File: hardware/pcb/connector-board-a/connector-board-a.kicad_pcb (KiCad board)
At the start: 2 copper layers, 23.1 x 39.1 mm, 2 parts, among them J1 DE9_Pins, J2 Conn_01x09_Pin

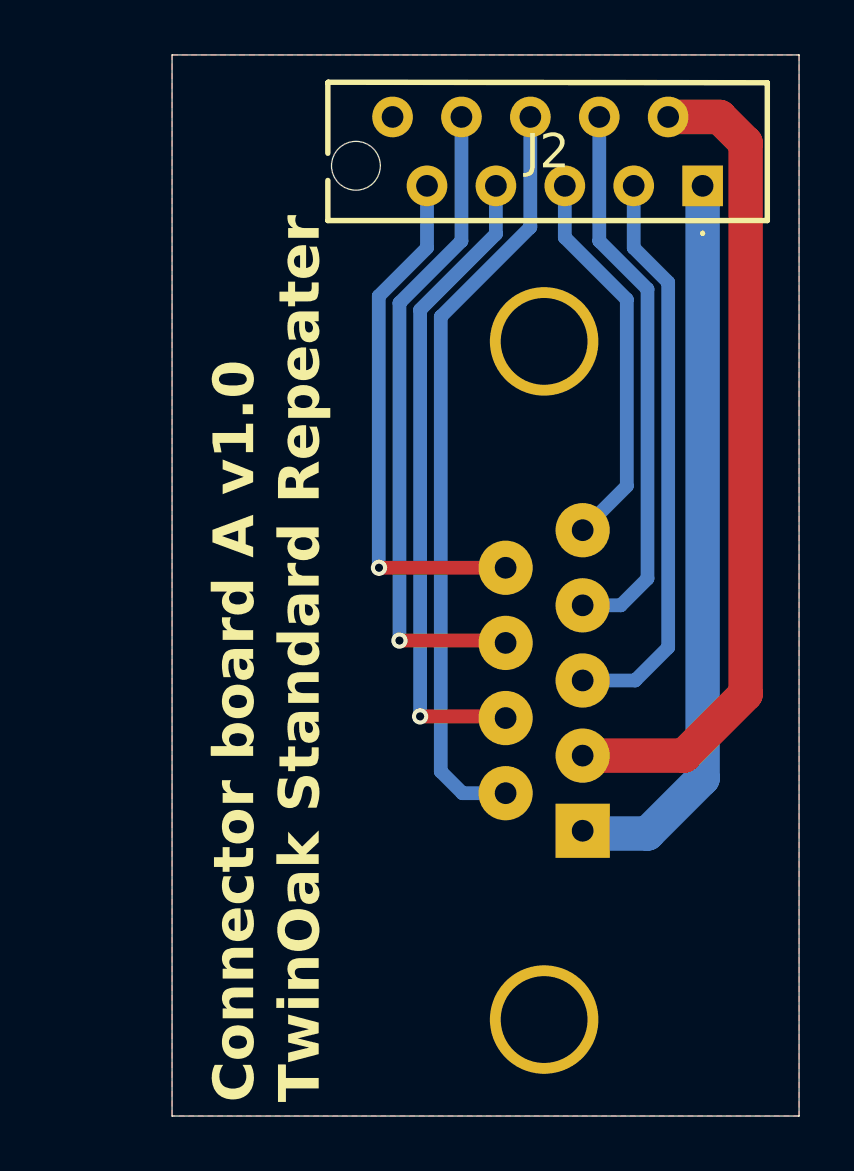
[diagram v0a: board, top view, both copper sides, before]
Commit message: Updated connector A board to rev 1.1
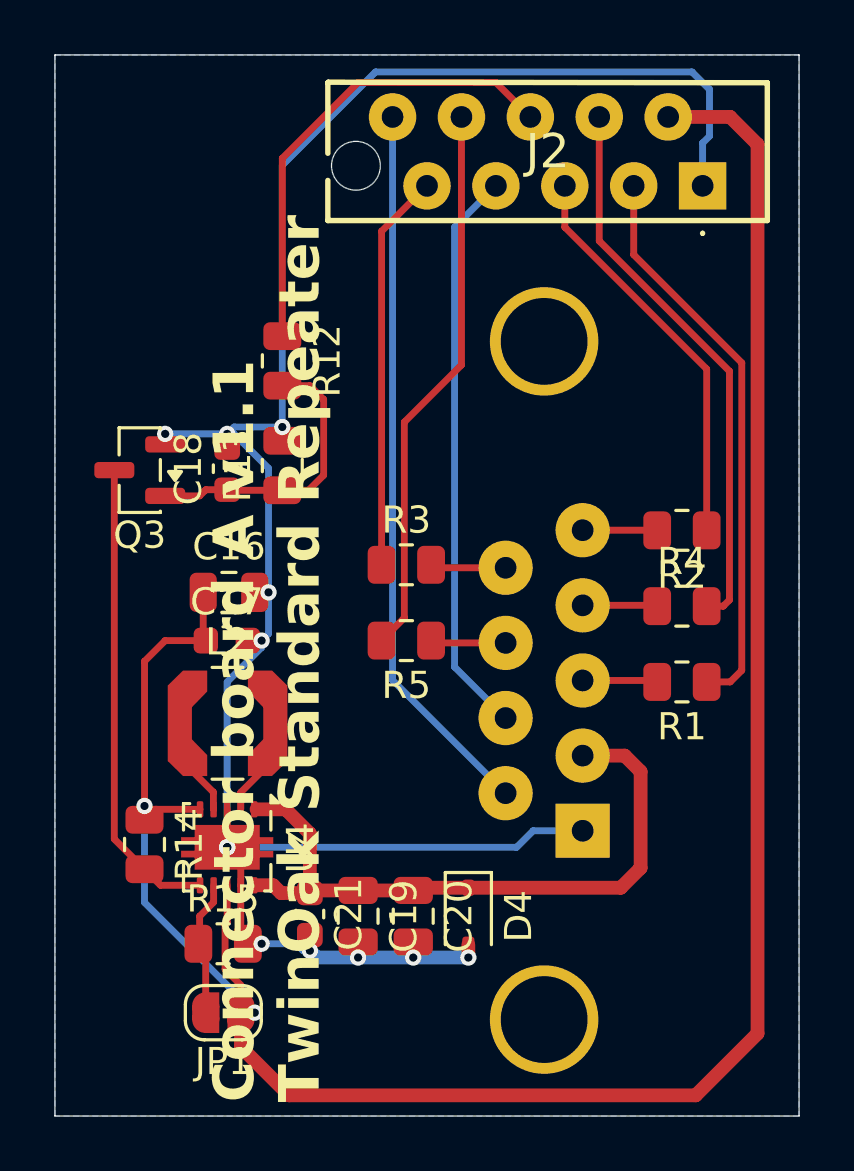
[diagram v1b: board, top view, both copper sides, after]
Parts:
- added C16: 10u, Capacitor_SMD:C_0805_2012Metric, F.Cu at (132.1, 91.4)
- added C17: 100n, Capacitor_SMD:C_0603_1608Metric, F.Cu at (132.1, 93.2)
- added C18: 1u, Capacitor_SMD:C_0603_1608Metric, F.Cu at (132.1, 86.9)
- added C19: 22u/10V, Capacitor_SMD:C_0805_2012Metric, F.Cu at (136.9, 103.4)
- added C20: 22u/10V, Capacitor_SMD:C_0805_2012Metric, F.Cu at (138.9, 103.4)
- added C21: 100n, Capacitor_SMD:C_0603_1608Metric, F.Cu at (135.1, 103.3)
- added D4: T03LC(DNP), Diode_SMD:D_SOD-323, F.Cu at (141.0, 103.4)
- added JP1: PWM, Jumper:SolderJumper-2_P1.3mm_Open_RoundedPad1.0x1.5mm, F.Cu at (131.9, 106.9)
- added L2: 2u2, Inductor_SMD:L_Coilcraft_LPS4018, F.Cu at (132.1, 96.3)
- added Q3: 2N7002, Package_TO_SOT_SMD:SOT-23, F.Cu at (128.9, 86.9)
- added R1: 470R, Resistor_SMD:R_0805_2012Metric, F.Cu at (148.8, 94.7)
- added R12: 10k, Resistor_SMD:R_0805_2012Metric, F.Cu at (134.1, 82.9)
- added R13: 100k, Resistor_SMD:R_0805_2012Metric, F.Cu at (134.1, 86.8)
- added R14: 100k, Resistor_SMD:R_0805_2012Metric, F.Cu at (129.0, 100.7)
- added R15: 100k, Resistor_SMD:R_0805_2012Metric, F.Cu at (131.9, 104.4)
- added R2: 470R, Resistor_SMD:R_0805_2012Metric, F.Cu at (148.8, 89.2)
- added R3: 470R, Resistor_SMD:R_0805_2012Metric, F.Cu at (138.7, 90.4)
- added R4: 470R, Resistor_SMD:R_0805_2012Metric, F.Cu at (148.8, 91.9)
- added R5: 470R, Resistor_SMD:R_0805_2012Metric, F.Cu at (138.7, 93.2)
- added U4: TPS63001, Package_SON:Texas_DRC0010J, F.Cu at (132.1, 100.8)
- J2: value Conn_01x09_Pin -> 8-215570-0
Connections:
- net Net-(J2-Pin_1) renamed GND
- net Net-(J2-Pin_7) renamed I2C_SDA
- J1 pad 2: Net-(J2-Pin_2) -> 3V3_LORA
- J1 pad 3: Net-(J2-Pin_3) -> LORA_nRESET
- J1 pad 4: Net-(J2-Pin_4) -> LORA_SWDCLK
- J1 pad 5: Net-(J2-Pin_5) -> LORA_SWDIO
- J1 pad 6: Net-(J2-Pin_6) -> I2C_SCL
- J1 pad 8: Net-(J2-Pin_8) -> WALTER_TX
- J1 pad 9: Net-(J2-Pin_9) -> WALTER_RX
- J2 pad 10: (no net) -> I2C_SCL
- J2 pad 2: Net-(J2-Pin_2) -> VBAT_RAW
- J2 pad 3: Net-(J2-Pin_3) -> Net-(J2-Pad3)
- J2 pad 4: Net-(J2-Pin_4) -> Net-(J2-Pad4)
- J2 pad 5: Net-(J2-Pin_5) -> Net-(J2-Pad5)
- J2 pad 6: Net-(J2-Pin_6) -> LORA_PWR_KILL
- J2 pad 8: Net-(J2-Pin_8) -> Net-(J2-Pad8)
- J2 pad 9: Net-(J2-Pin_9) -> Net-(J2-Pad9)
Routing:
- net VBAT_RAW: track 0.00 -> 85.7 mm, vias 0 -> 2
- net GND: track 27.1 -> 83.4 mm, vias 0 -> 12
- net Net-(J2-Pin_2): track 30.5 -> 0.00 mm
- net Net-(J2-Pin_6): track 28.2 -> 0.00 mm
- net I2C_SCL: track 0.00 -> 26.7 mm
- net 3V3_LORA: track 0.00 -> 25.1 mm
- net Net-(J2-Pin_8): track 24.2 -> 0.00 mm, vias 1 -> 0
- net Net-(J2-Pin_3): track 21.2 -> 0.00 mm
- net Net-(J2-Pad3): track 0.00 -> 21.0 mm
- net Net-(J2-Pad4): track 0.00 -> 20.7 mm
- net Net-(J2-Pin_4): track 20.6 -> 0.00 mm
- net Net-(J2-Pad8): track 0.00 -> 20.5 mm
- net Net-(J2-Pin_9): track 19.5 -> 0.00 mm, vias 1 -> 0
- net Net-(Q3-D): track 0.00 -> 17.5 mm
- net LORA_PWR_KILL: track 0.00 -> 17.4 mm
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- added copper zone on B.Cu, net GND
- removed copper zone on F.Cu, net GND
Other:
- board size 23.1 x 39.1 mm -> 27.4 x 39.1 mm
- board text added: "Connector board A v1.1 TwinOak Standard Repeater"
- board text removed: "Connector board A v1.0 TwinOak Standard Repeater"
